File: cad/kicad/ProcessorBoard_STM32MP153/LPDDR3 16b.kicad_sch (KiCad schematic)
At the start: 6 parts, among them IC401 IS43LD16320A-25BLI

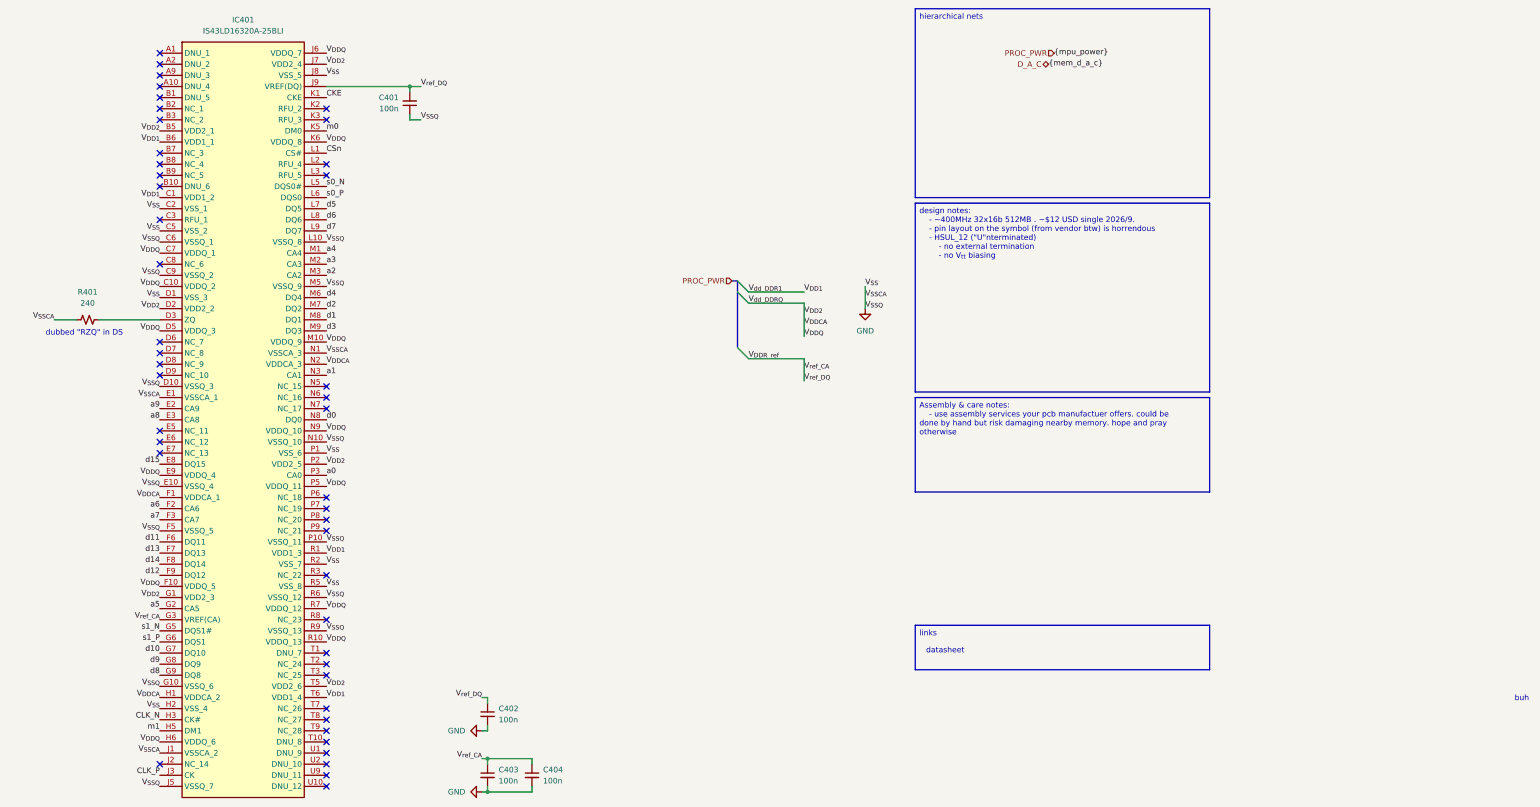
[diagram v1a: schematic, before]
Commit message: new ram
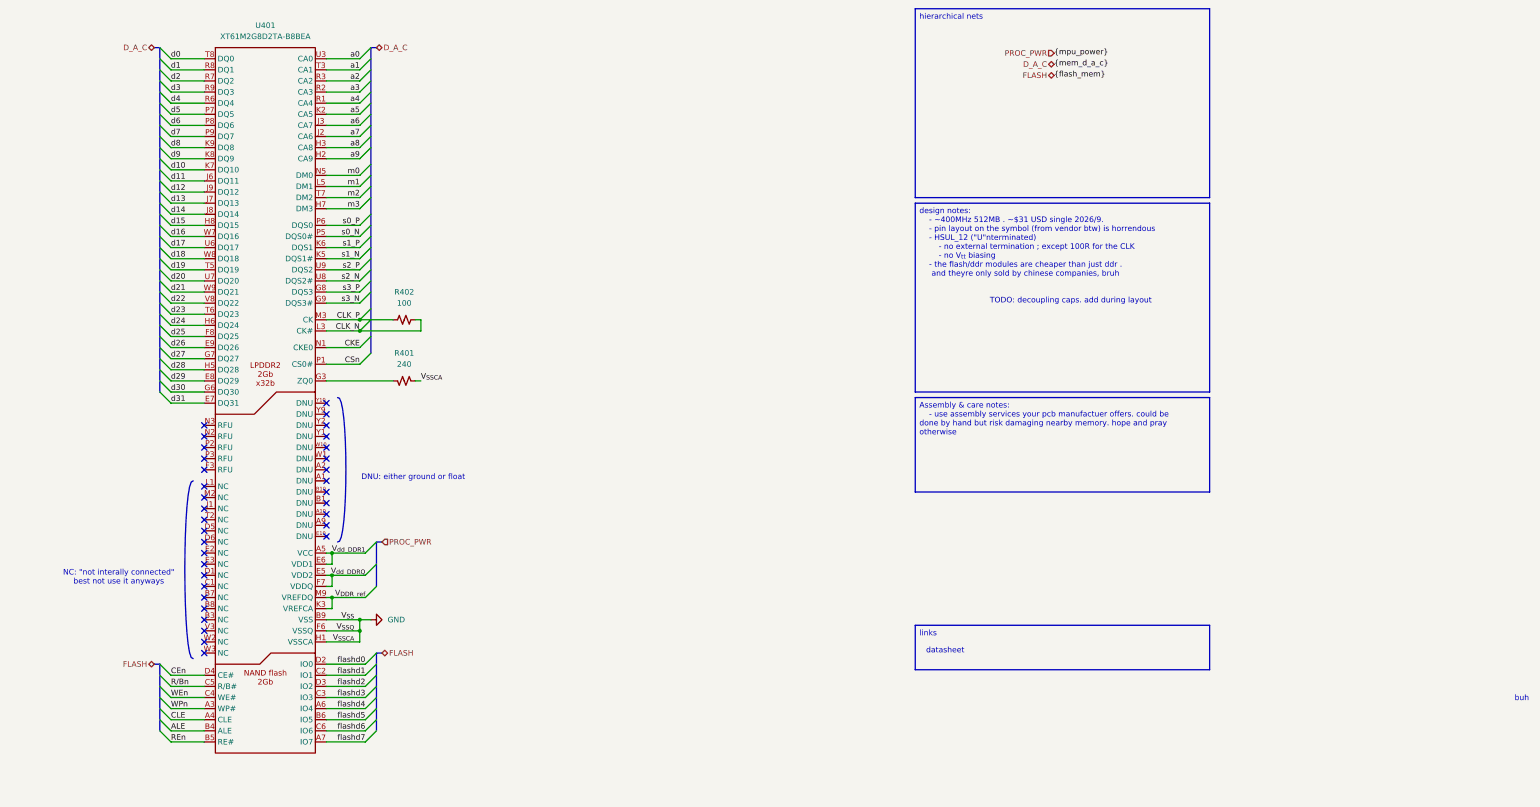
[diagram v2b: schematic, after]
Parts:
- removed C401, C402, C403, C404: 100n, Capacitor_SMD:C_0402_1005Metric_Pad0.74x0.62mm_HandSolder, symbol Device:C_Small
- removed IC401: IS43LD16320A-25BLI, __WM_Local:BGA134C65P10X17_1000X1150X110, symbol __WM_Local:IS43LD16320A-25BLI
- added R402: 100, Resistor_SMD:R_0402_1005Metric_Pad0.72x0.64mm_HandSolder, symbol Device:R_Small_US
- added U401: XT61M2G8D2TA-B8BEA, __WM_Local:FBGA-162_L10.5-W8.0-P0.50_XT61M4G8D2TA, symbol __WM_Local:XT61M2G8D2TA-B8BEA
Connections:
- net CKE: now also U401.N1 (CKE0)
- net CLK_N: now also R402.2, U401.L3 (CK#)
- net CLK_P: now also R402.1, U401.M3 (CK)
- net CSn: now also U401.P1 (CS0#)
- net GND: now also R401.2, U401.B9 (VSS), U401.E1 (VSS), U401.F2 (VSS), U401.F5 (VSS), U401.F6 (VSSQ), U401.F9 (VSSQ), U401.G1 (VSS), U401.G10 (VSSQ), U401.H1 (VSSCA), U401.H10 (VSSQ), U401.J5 (VSSQ), U401.K10 (VSSQ), U401.L2 (VSS), U401.M1 (VSSCA), U401.M5 (VSSQ), U401.M8 (VSS), U401.P10 (VSSQ), U401.R5 (VSSQ), U401.T1 (VSSCA), U401.T10 (VSSQ), U401.U1 (VSS), U401.U10 (VSSQ), U401.V2 (VSS), U401.V5 (VSS), U401.V6 (VSSQ), U401.V9 (VSSQ); no longer R401.1
- net V_{DDR_ref}: now also U401.K3 (VREFCA), U401.M9 (VREFDQ)
- net a0: now also U401.U3 (CA0)
- net a1: now also U401.T3 (CA1)
- net a2: now also U401.R3 (CA2)
- net a3: now also U401.R2 (CA3)
- net a4: now also U401.R1 (CA4)
- net a5: now also U401.K2 (CA5)
- net a6: now also U401.J3 (CA7)
- net a7: now also U401.J2 (CA6)
- net a8: now also U401.H3 (CA8)
- net a9: now also U401.H2 (CA9)
- net d0: now also U401.T8 (DQ0)
- net d1: now also U401.R8 (DQ1)
- net d10: now also U401.K7 (DQ10)
- net d11: now also U401.J6 (DQ11)
- net d12: now also U401.J9 (DQ12)
- net d13: now also U401.J7 (DQ13)
- net d14: now also U401.J8 (DQ14)
- net d15: now also U401.H8 (DQ15)
- net d2: now also U401.R7 (DQ2)
- net d3: now also U401.R9 (DQ3)
- net d4: now also U401.R6 (DQ4)
- net d5: now also U401.P7 (DQ5)
- net d6: now also U401.P8 (DQ6)
- net d7: now also U401.P9 (DQ7)
- net d8: now also U401.K9 (DQ8)
- net d9: now also U401.K8 (DQ9)
- net m0: now also U401.N5 (DM0)
- net m1: now also U401.L5 (DM1)
- net s0_N: now also U401.P5 (DQS0#)
- net s0_P: now also U401.P6 (DQS0)
- net s1_N: now also U401.K5 (DQS1#)
- net s1_P: now also U401.K6 (DQS1)
- new net: R401.1, U401.G3 (ZQ0)
- new net ALE: U401.B4 (ALE)
- new net CEn: U401.D4 (CE#)
- new net CLE: U401.A4 (CLE)
- new net REn: U401.B5 (RE#)
- new net R/Bn: U401.C5 (R/B#)
- new net V_{dd_DDR1}: U401.A5 (VCC), U401.A8 (VCC), U401.B2 (VCC), U401.E6 (VDD1), U401.F1 (VDD1), U401.V1 (VDD1), U401.W6 (VDD1)
- new net V_{dd_DDRQ}: U401.E5 (VDD2), U401.F10 (VDDQ), U401.F7 (VDDQ), U401.G2 (VDD2), U401.G5 (VDDQ), U401.H9 (VDDQ), U401.J10 (VDDQ), U401.K1 (VDD2), U401.L6 (VDDQ), U401.M6 (VDDQ), U401.M7 (VDD2), U401.N6 (VDDQ), U401.R10 (VDDQ), U401.T9 (VDDQ), U401.U2 (VDD2), U401.U5 (VDDQ), U401.V10 (VDDQ), U401.V7 (VDDQ), U401.W5 (VDD2)
- new net WEn: U401.C4 (WE#)
- new net WPn: U401.A3 (WP#)
- new net d16: U401.W7 (DQ16)
- new net d17: U401.U6 (DQ17)
- new net d18: U401.W8 (DQ18)
- new net d19: U401.T5 (DQ19)
- new net d20: U401.U7 (DQ20)
- new net d21: U401.W9 (DQ21)
- new net d22: U401.V8 (DQ22)
- new net d23: U401.T6 (DQ23)
- new net d24: U401.H6 (DQ24)
- new net d25: U401.F8 (DQ25)
- new net d26: U401.E9 (DQ26)
- new net d27: U401.G7 (DQ27)
- new net d28: U401.H5 (DQ28)
- new net d29: U401.E8 (DQ29)
- new net d30: U401.G6 (DQ30)
- new net d31: U401.E7 (DQ31)
- new net flashd0: U401.D2 (IO0)
- new net flashd1: U401.C2 (IO1)
- new net flashd2: U401.D3 (IO2)
- new net flashd3: U401.C3 (IO3)
- new net flashd4: U401.A6 (IO4)
- new net flashd5: U401.B6 (IO5)
- new net flashd6: U401.C6 (IO6)
- new net flashd7: U401.A7 (IO7)
- new net m2: U401.T7 (DM2)
- new net m3: U401.H7 (DM3)
- new net s2_N: U401.U8 (DQS2#)
- new net s2_P: U401.U9 (DQS2)
- new net s3_N: U401.G9 (DQS3#)
- new net s3_P: U401.G8 (DQS3)
- no-connect marks 45 -> 34
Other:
- note added: "DNU: either ground or float"
- note added: "NC: "not interally connected" best not use it anyways"
- note added: "TODO: decoupling caps. add during layout"
- note removed: "dubbed "RZQ" in DS"
- moved on the sheet: R401

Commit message: realtek bridge thing somewhat more wired
apparently the proper term for via skimping and what not is NFPR (non functional pad removal). all my homies love NFPR. so it is possible to route 0.5mm bga. still fighting the dog but at least cant bring it to another layer
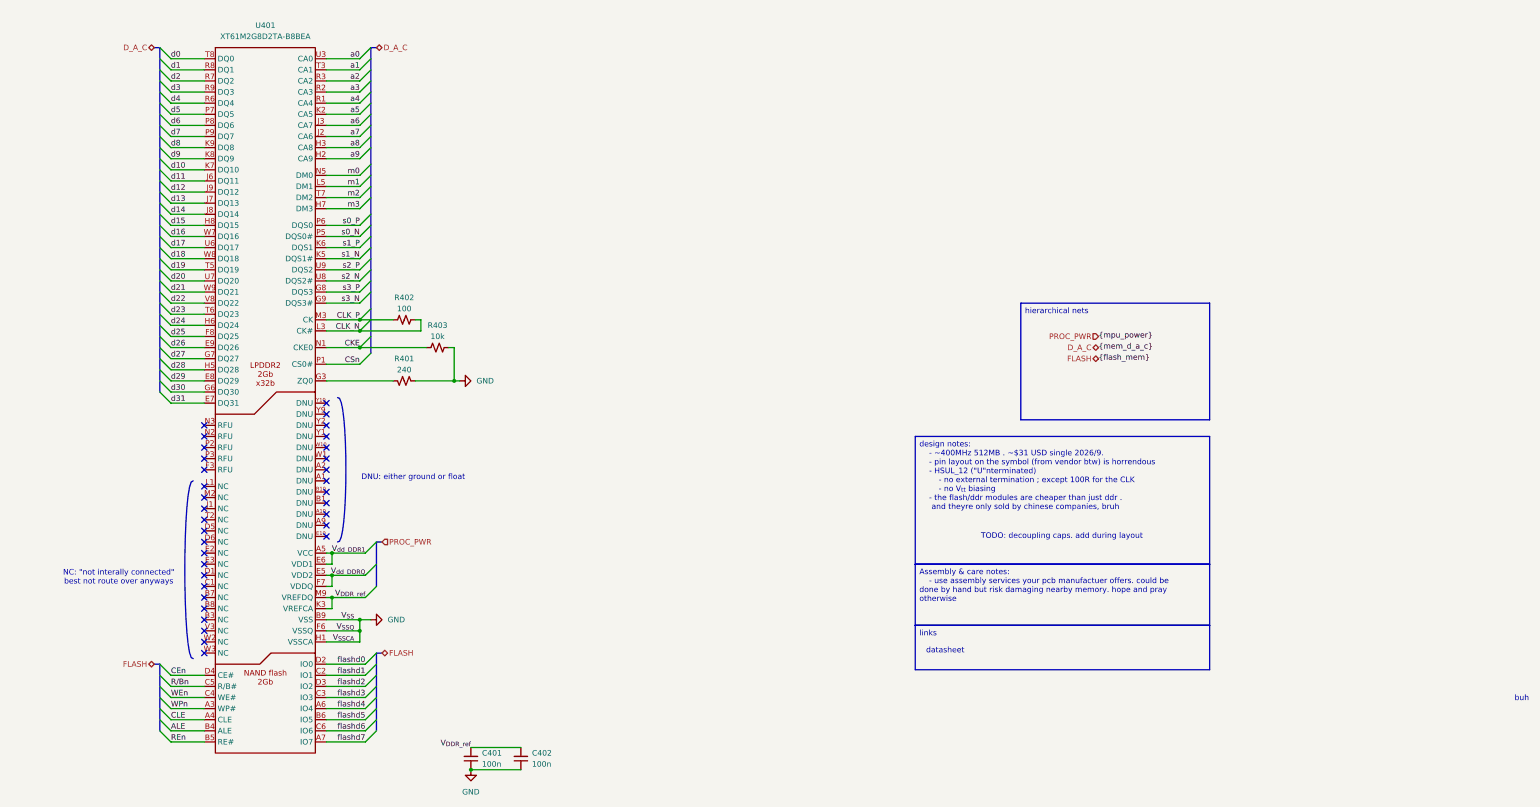
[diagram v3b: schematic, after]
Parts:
- added C401, C402: 100n, Capacitor_SMD:C_0402_1005Metric_Pad0.74x0.62mm_HandSolder, symbol Device:C_Small
- added R403: 10k, Resistor_SMD:R_0603_1608Metric_Pad0.98x0.95mm_HandSolder, symbol Device:R_Small_US
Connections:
- net CKE: now also R403.1
- net GND: now also C401.1, C402.1, R403.2
- net V_{DDR_ref}: now also C401.2, C402.2
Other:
- note added: "NC: "not interally connected" best not route over anyways"
- note removed: "NC: "not interally connected" best not use it anyways"

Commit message: miled fixes
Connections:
- net a6: now also U401.J2 (CA6); no longer U401.J3 (CA7)
- net a7: now also U401.J3 (CA7); no longer U401.J2 (CA6)
- net s2_N: now also U401.U9 (DQS2#); no longer U401.U8 (DQS2#)
- net s2_P: now also U401.U8 (DQS2); no longer U401.U9 (DQS2)
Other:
- note added: "NAND for persistent storage only; NOT bootable. is not powered on boot."
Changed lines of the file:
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@@
 	(bezier
 		(pts
-			(xy 50.8 162.56) (xy 48.26 163.83) (xy 48.26 120.65) (xy 50.8 121.92)
+			(xy 50.8 162.56) (xy 48.26 163.83) (xy 48.26 128.27) (xy 50.8 129.54)
 		)
 		(stroke
@@
 		)
 	)
-	(text_box "design notes:\n	- ~400MHz 512MB . ~$31 USD single 2026/9. \n	- pin layout on the symbol (from vendor btw) is horrendous\n	- HSUL_12 (\"U\"nterminated)\n		- no external termination ; except 100R for the CLK\n		- no V_{tt} biasing\n	- the flash/ddr modules are cheaper than just ddr . \n	 and theyre only sold by chinese companies, bruh"
+	(text "NAND for persistent storage only; NOT bootable. \nis not powered on boot."
+		(exclude_from_sim no)
+		(at 68.58 188.214 0)
+		(effects
+			(font
+				(size 1.27 1.27)
+			)
+		)
+	)
+	(text_box "design notes:\n	- 400MHz 512MB . ~$31 USD single 2026/9. \n	- HSUL_12 (\"U\"nterminated)\n		- no external termination ; except 100R for the CLK\n		- no V_{tt} biasing\n	- the flash/ddr modules are cheaper than just ddr . \n	 but only chinese companies have them stocked, bruh"
 		(exclude_from_sim no)
 		(at 215.9 111.76 0)
@@
 	)
 	(no_connect
+		(at 53.34 127)
+	)
+	(no_connect
 		(at 53.34 109.22)
 	)
@@
 	)
 	(no_connect
-		(at 53.34 125.73)
-	)
-	(no_connect
-		(at 53.34 128.27)
-	)
-	(no_connect
 		(at 81.28 111.76)
 	)
@@
 	)
 	(no_connect
+		(at 53.34 121.92)
+	)
+	(no_connect
+		(at 53.34 124.46)
+	)
+	(no_connect
 		(at 53.34 143.51)
 	)
@@
 	)
 	(no_connect
-		(at 53.34 123.19)
-	)
-	(no_connect

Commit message: double inversion trap
the crab has a double inversion, the pins internal logic is inverted. and the output logic-high is dynamically determined. bruh
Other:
- note added: "NAND for persistent storage only; NOT bootable due to powered sequence. possible but not implimented"
- note removed: "NAND for persistent storage only; NOT bootable. is not powered on boot."
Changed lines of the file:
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@@
 		)
 	)
-	(text "NAND for persistent storage only; NOT bootable. \nis not powered on boot."
+	(text "NAND for persistent storage only; NOT bootable\ndue to powered sequence. possible but not implimented"
 		(exclude_from_sim no)
 		(at 68.58 188.214 0)

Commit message: all hail the auto router
https://ih1.redbubble.net/image.6083290940.2638/flat,750x,075,f-pad,750x1000,f8f8f8.jpg
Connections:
- net CKE renamed ddr.CKE
- net CLK_N renamed ddr.CLK_N
- net CLK_P renamed ddr.CLK_P
- net CSn renamed ddr.CSn
- net a0 renamed ddr.a0
- net a1 renamed ddr.a1
- net a2 renamed ddr.a2
- net a3 renamed ddr.a3
- net a4 renamed ddr.a4
- net a5 renamed ddr.a5
- net a6 renamed ddr.a6
- net a7 renamed ddr.a7
- net a8 renamed ddr.a8
- net a9 renamed ddr.a9
- net d0 renamed ddr.d0
- net d1 renamed ddr.d1
- net d10 renamed ddr.d10
- net d11 renamed ddr.d11
- net d12 renamed ddr.d12
- net d13 renamed ddr.d13
- net d14 renamed ddr.d14
- net d15 renamed ddr.d15
- net d16 renamed ddr.d16
- net d17 renamed ddr.d17
- net d18 renamed ddr.d18
- net d19 renamed ddr.d19
- net d2 renamed ddr.d2
- net d20 renamed ddr.d20
- net d21 renamed ddr.d21
- net d22 renamed ddr.d22
- net d23 renamed ddr.d23
- net d24 renamed ddr.d24
- net d25 renamed ddr.d25
- net d26 renamed ddr.d26
- net d27 renamed ddr.d27
- net d28 renamed ddr.d28
- net d29 renamed ddr.d29
- net d3 renamed ddr.d3
- net d30 renamed ddr.d30
- net d31 renamed ddr.d31
- net d4 renamed ddr.d4
- net d5 renamed ddr.d5
- net d6 renamed ddr.d6
- net d7 renamed ddr.d7
- net d8 renamed ddr.d8
- net d9 renamed ddr.d9
- net m0 renamed ddr.m0
- net m1 renamed ddr.m1
- net m2 renamed ddr.m2
- net m3 renamed ddr.m3
- net s0_N renamed ddr.s0_N
- net s0_P renamed ddr.s0_P
- net s1_N renamed ddr.s1_N
- net s1_P renamed ddr.s1_P
- net s2_N renamed ddr.s2_N
- net s2_P renamed ddr.s2_P
- net s3_N renamed ddr.s3_N
- net s3_P renamed ddr.s3_P
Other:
- moved on the sheet: R401, R402, R403

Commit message: somewhat fanned
the auto router sucks :( . and the auto fanout sucks. and i routed everything on the wrong grid and it snapped to teh wrong places and i only noticed most of teh way though so i push and make it tomorrows problem
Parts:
- renumbered R402 to R401, R401 to R402
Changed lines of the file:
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@@
 		(in_pos_files yes)
 		(dnp no)
-		(property "Reference" "R401"
+		(property "Reference" "R402"
 			(at 102.87 93.98 90)
 			(show_name no)
@@
 			(project "ProcessorBoard_STM32MP153"
 				(path "/e63e39d7-6ac0-4ffd-8aa3-1841a4541b55/fb747675-6d29-4589-92ae-6726c227ffd0"
-					(reference "R401")
+					(reference "R402")
 					(unit 1)
 				)
@@
 		(in_pos_files yes)
 		(dnp no)
-		(property "Reference" "R402"
+		(property "Reference" "R401"
 			(at 102.87 80.01 90)
 			(show_name no)
@@
 			(project "ProcessorBoard_STM32MP153"
 				(path "/e63e39d7-6ac0-4ffd-8aa3-1841a4541b55/fb747675-6d29-4589-92ae-6726c227ffd0"
-					(reference "R402")
+					(reference "R401")
 					(unit 1)
 				)

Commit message: where ram :(
its 56 connecitons (not including pwr and gnd) for x32 bus. not possible witout HDI or increasing layer count, both are big bucks. so long china ram. apparently winabond has some hidden gems and ebay smugglers as a supply chain. good stuff. and micron gatekeeps theyre datasheets.
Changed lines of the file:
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@@
 		)
 	)
-	(text_box "design notes:\n	- 400MHz 512MB . ~$31 USD single 2026/9. \n	- HSUL_12 (\"U\"nterminated)\n		- no external termination ; except 100R for the CLK\n		- no V_{tt} biasing\n	- the flash/ddr modules are cheaper than just ddr . \n	 but only chinese companies have them stocked, bruh"
+	(text_box "design notes:\n	- 400MHz 512MB x32. ~$31 USD single 2026/9. \n	- HSUL_12 (\"U\"nterminated)\n		- no external termination ; except 100R for the CLK\n		- no V_{tt} biasing\n	- the flash/ddr modules are cheaper than just ddr . \n	 but only chinese companies have them stocked, bruh"
 		(exclude_from_sim no)
 		(at 215.9 111.76 0)
